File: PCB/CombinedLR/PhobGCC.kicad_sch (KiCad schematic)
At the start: 82 parts, among them J1 Conn_01x06_Female, J2 Conn_01x04_Female, J3 Conn_01x01_Male, J4 Conn_01x04_Male, J5 Conn_01x02_Male, J6 Conn_01x02_Male, J7 Conn_01x02_Male, Q1 Q_NMOS_GSD, Q2 Q_PMOS_GDS, Q3 Q_NMOS_GSD, SW1 A, SW10 Dup, SW11 Dright, SW12 Ddown, SW13 L, SW14 R, SW2 B, SW3 X, SW4 Y, SW5 Start, SW6 L, SW7 R, SW8 1825027-5, SW9 Dleft, U1 Teensy4.0, U2 2x DRV5053CAQLPGM Hall Effect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, U3 GP2S60-MFG, U4 GP2S60-MFG, U5 Stickbox_Assembly

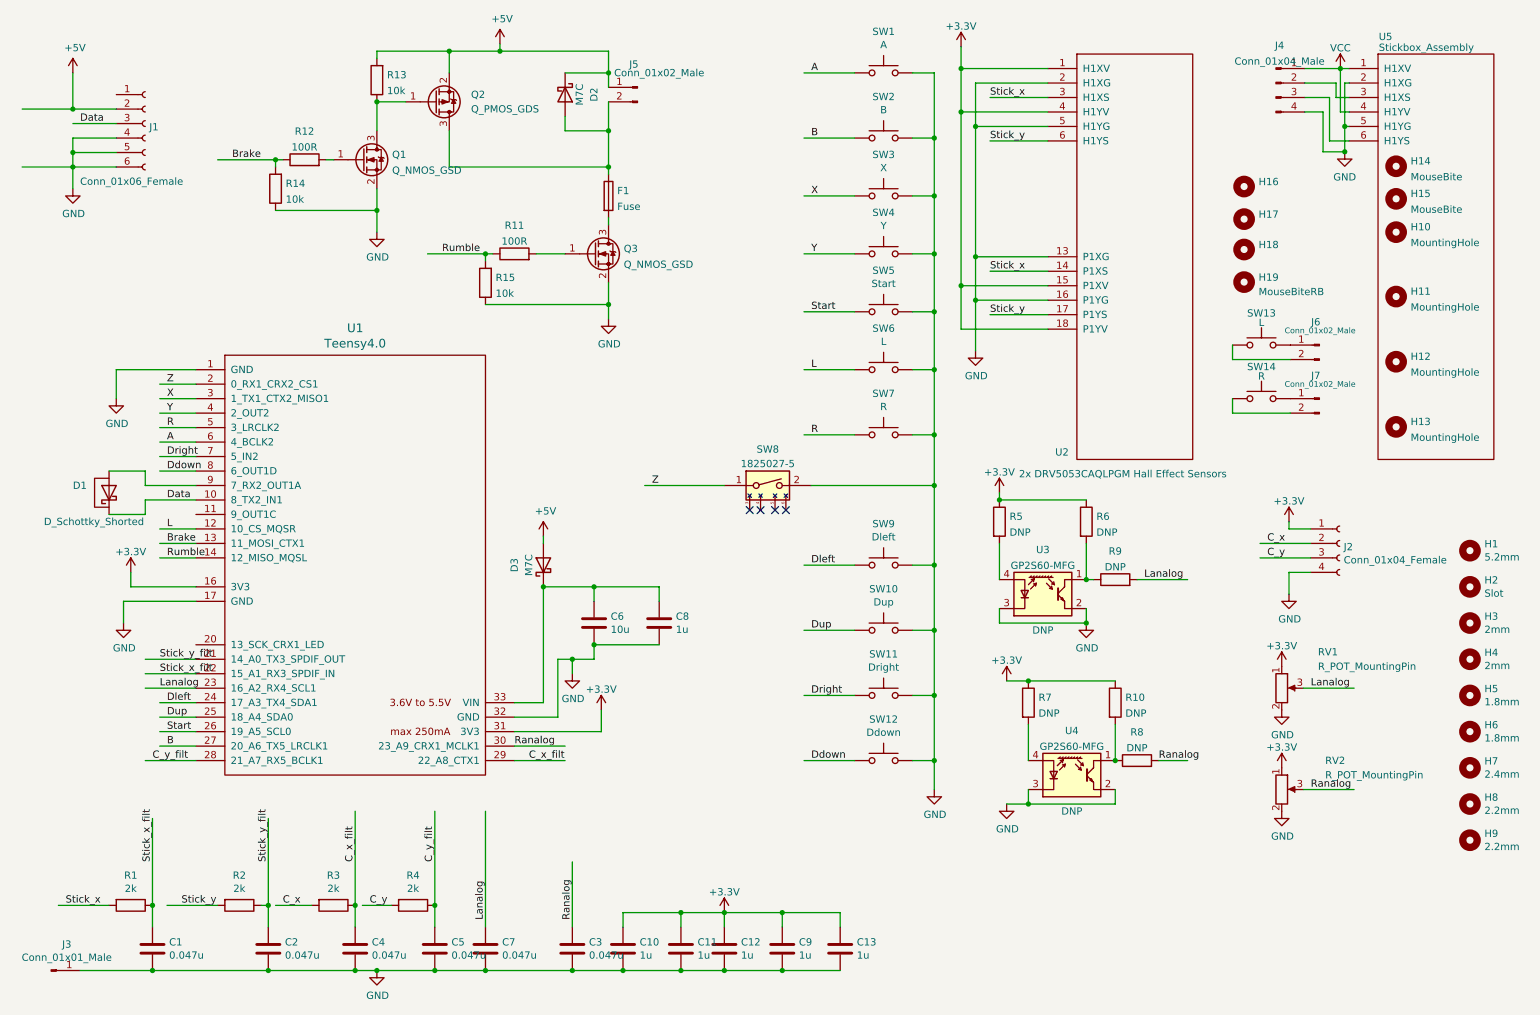
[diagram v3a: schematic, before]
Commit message: swapped fuse, fixed LR
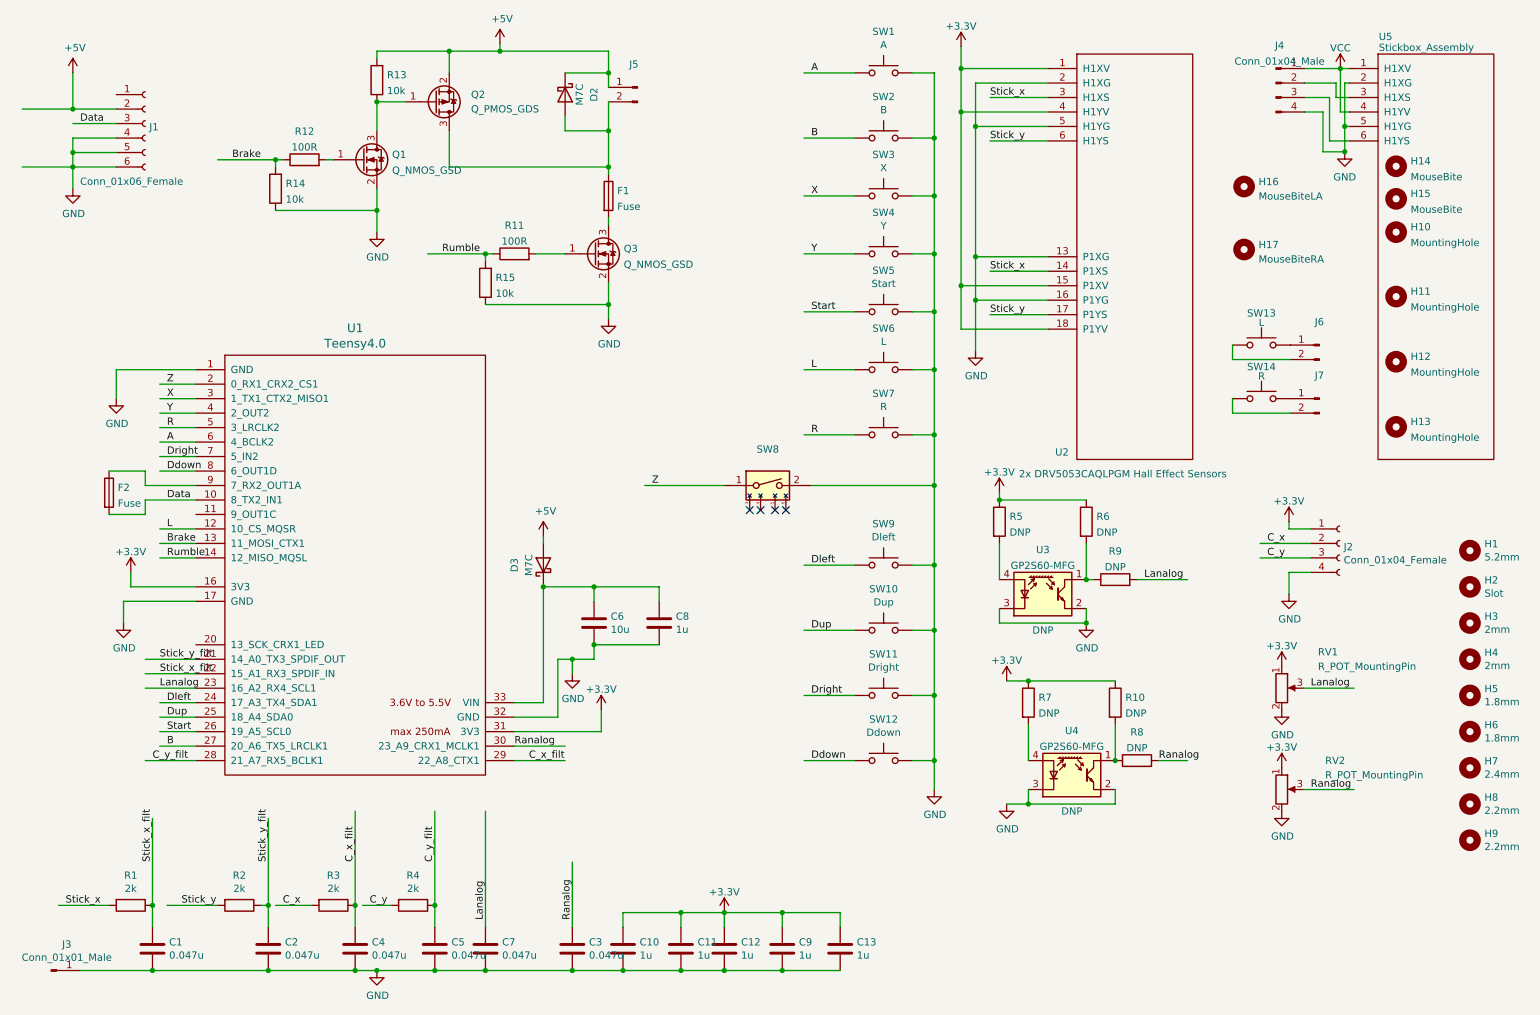
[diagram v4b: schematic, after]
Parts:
- removed D1: D_Schottky_Shorted, Gamecube MB:D_SOD-523_Shorted, symbol Gamecube MB:D_Schottky_Shorted
- removed H17: (no value), PhobGCC_Footprints:breakaway-mousebites, symbol Mechanical:MountingHole
- removed H19: MouseBiteRB, PhobGCC_Footprints:breakaway-mousebites, symbol Mechanical:MountingHole
- added F2: Fuse, Resistor_SMD:R_1206_3216Metric, symbol Device:Fuse
- H14, H15: footprint PhobGCC_Footprints:mouse-bite-2.54mm-slot -> (none)
- H16: value (none) -> MouseBiteLA; footprint PhobGCC_Footprints:breakaway-mousebites -> (none)
- H17: renamed from H18; value (none) -> MouseBiteRA; footprint PhobGCC_Footprints:breakaway-mousebites -> (none)
- J5, J6, J7: value Conn_01x02_Male -> (none); footprint Connector_PinHeader_2.54mm:PinHeader_1x02_P2.54mm_Vertical -> (none)
- SW6, SW7: footprint Pin_Headers:Pin_Header_Straight_1x02_Pitch2.54mm -> (none)
- SW8: value 1825027-5 -> (none)
- U1: footprint teensy:Teensy40_Edge_Pins -> (none)
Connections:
- net Data: now also F2.2
- net at U1.9 (7_RX2_OUT1A): now also F2.1

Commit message: wide mousebites
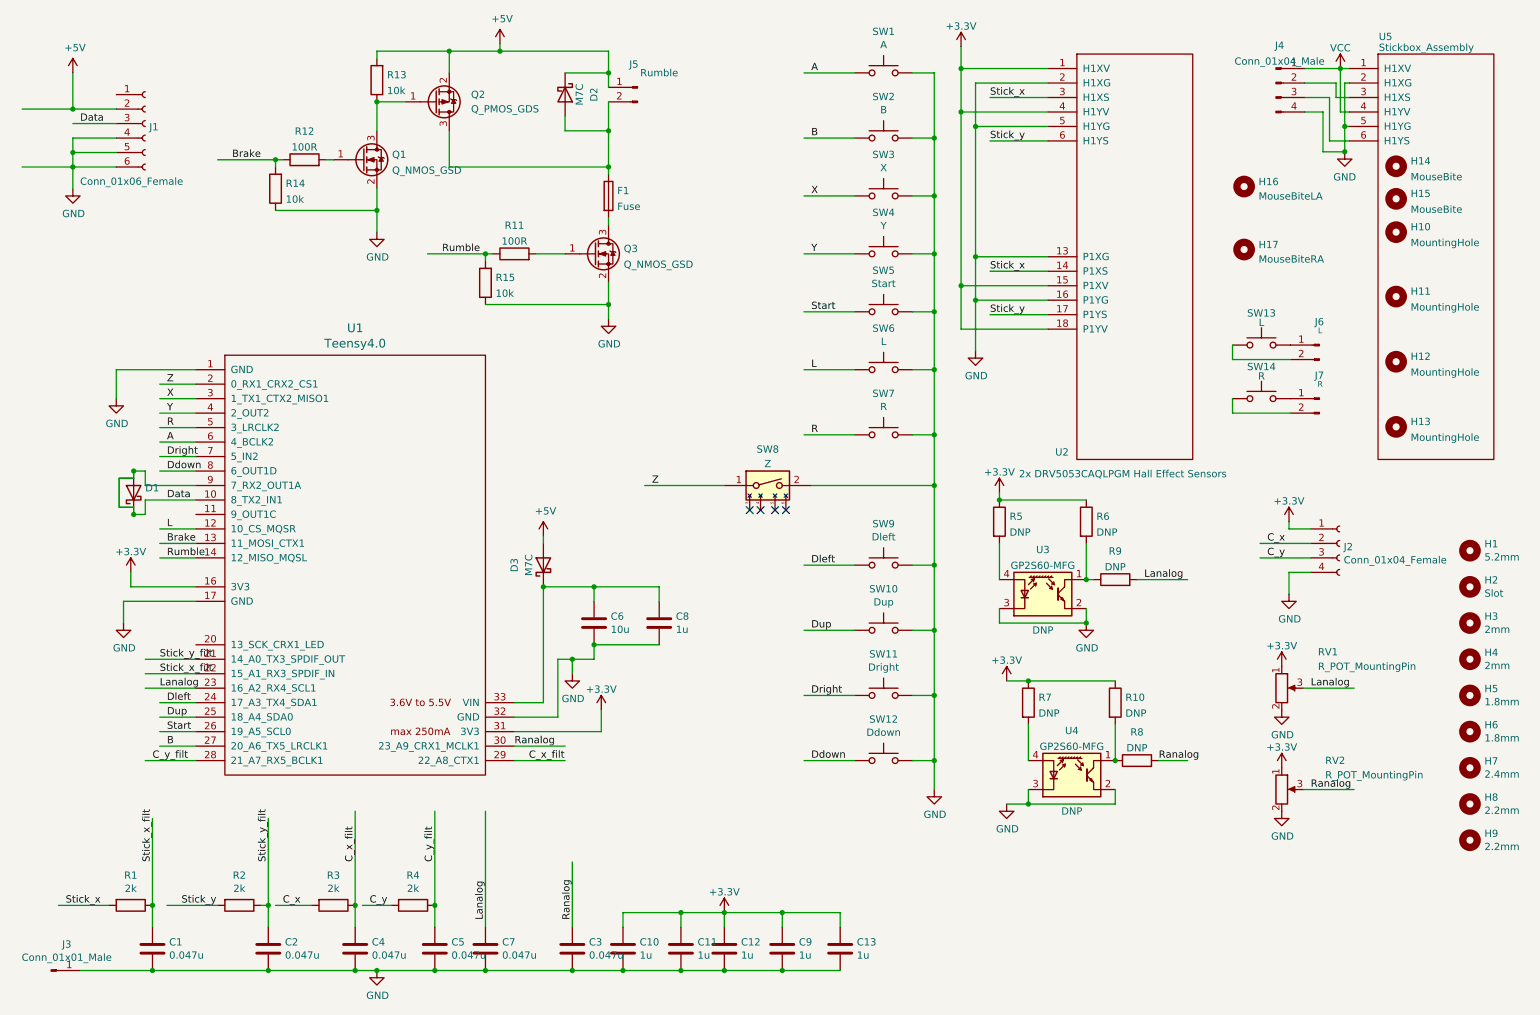
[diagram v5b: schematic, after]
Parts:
- removed F2: Fuse, Resistor_SMD:R_1206_3216Metric, symbol Device:Fuse
- added D1: (no value), symbol PhobGCC_Symbol_Library:D_Schottky_Shorted
- H14, H15, H16, H17: footprint (none) -> PhobGCC_Footprints:breakaway-mousebites-double
- J5: value (none) -> Rumble; footprint (none) -> PhobGCC_Footprints:Pin_Header_Straight_1x02_Pitch2.54mm
- J6: value (none) -> L; footprint (none) -> PhobGCC_Footprints:Pin_Header_Straight_1x02_Pitch2.54mm
- J7: value (none) -> R; footprint (none) -> PhobGCC_Footprints:Pin_Header_Straight_1x02_Pitch2.54mm
- SW6, SW7: footprint (none) -> PhobGCC_Footprints:Pin_Header_Straight_1x02_Pitch2.54mm
- SW8: value (none) -> Z
- U1: footprint (none) -> PhobGCC_Footprints:Teensy40_Edge_Pins
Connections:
- net Data: now also U1.9 (7_RX2_OUT1A), D1.1 (K), D1.2 (A)
